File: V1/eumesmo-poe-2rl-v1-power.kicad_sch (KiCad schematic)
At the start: 31 parts, among them U4 TPS2376DDAR-H, U5 TX4138, U6 SY8089A1AAC

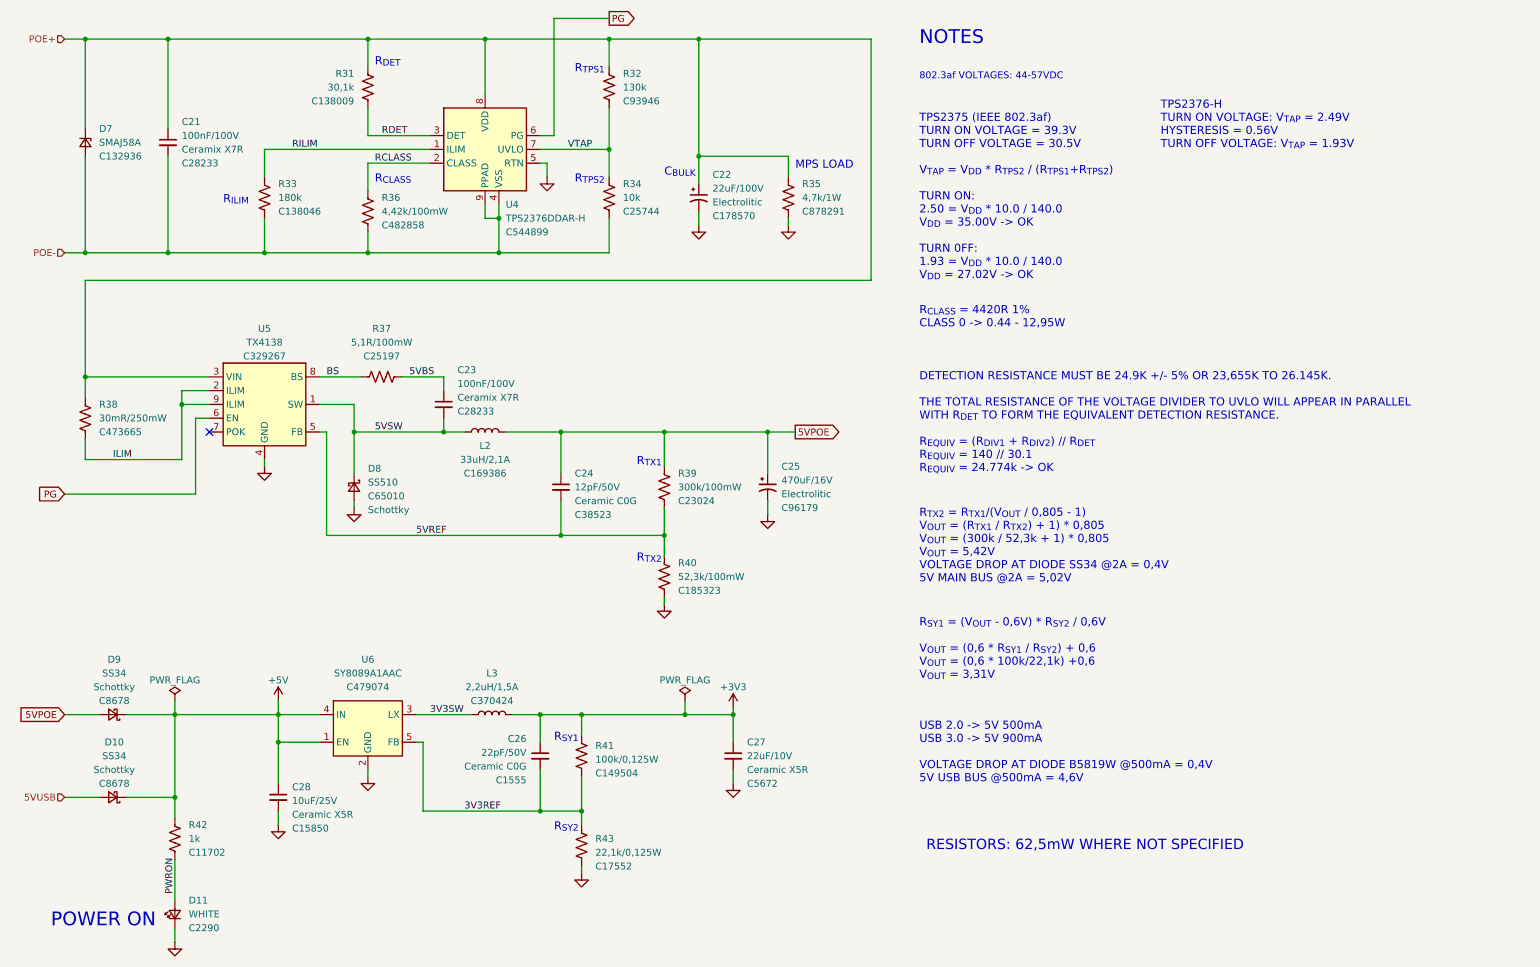
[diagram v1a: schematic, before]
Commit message: Added CPU health LED
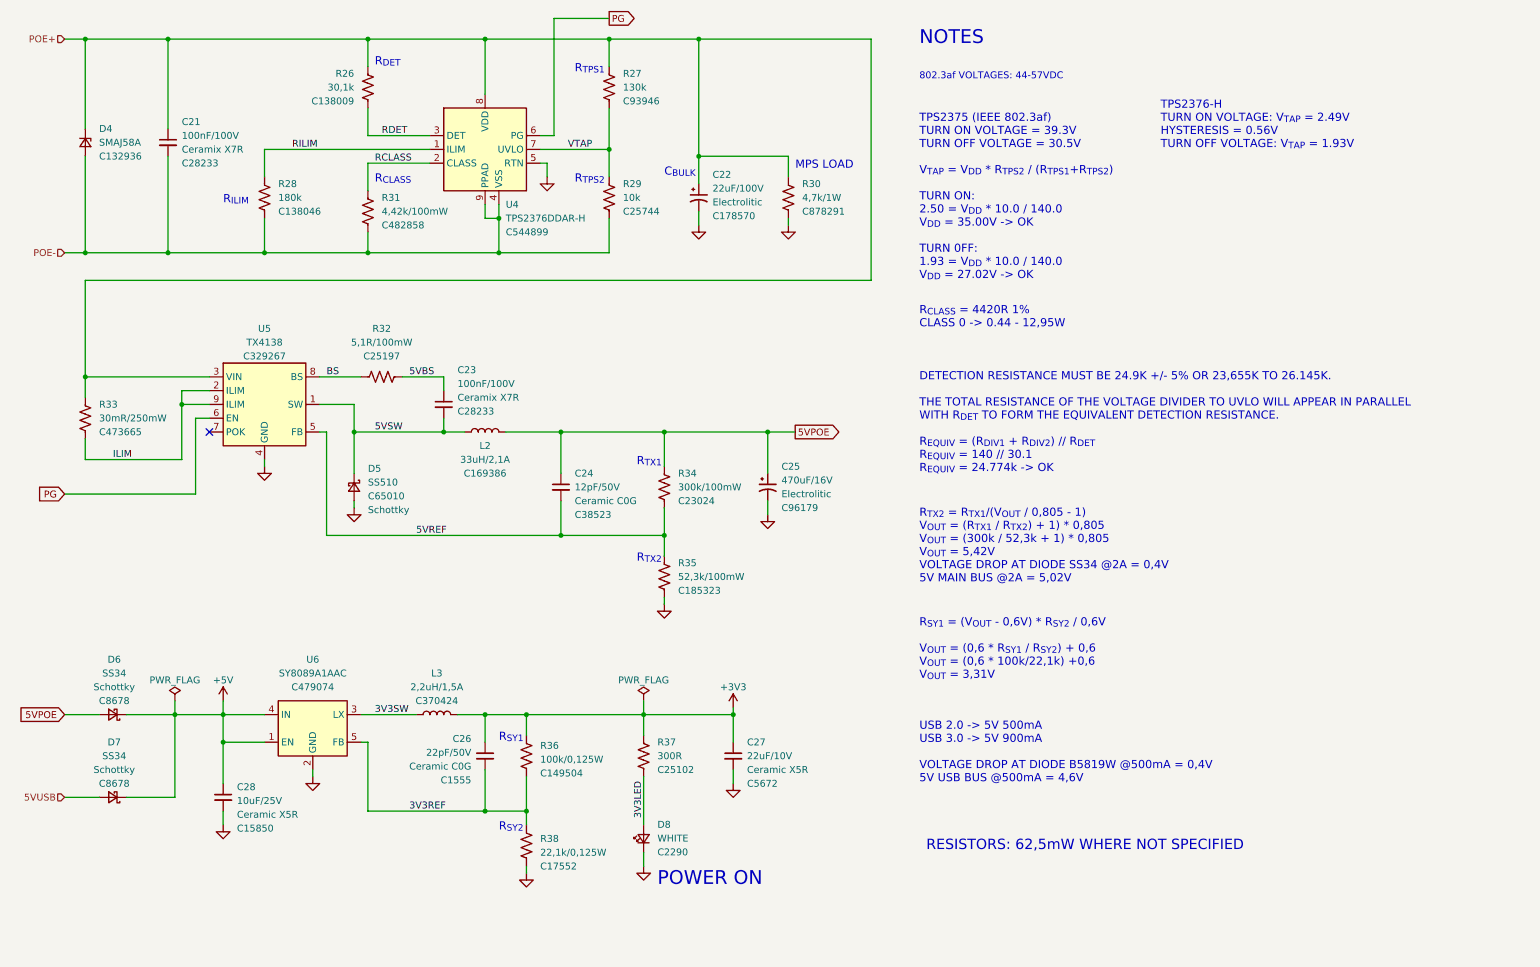
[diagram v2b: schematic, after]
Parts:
- removed D11: WHITE, Tales:LED_0603_1608Metric, symbol Device:LED_Small
- removed R42: 1k, Tales:R_0402_1005Metric, symbol Device:R_US
- added D8: WHITE, Tales:LED_0603_1608Metric, symbol Device:LED_Small
- added R37: 300R, Tales:R_0402_1005Metric, symbol Device:R_US
- renumbered D7 to D4, D8 to D5, D9 to D6, D10 to D7, R31 to R26, R32 to R27, R33 to R28, R34 to R29, R35 to R30, R36 to R31, R37 to R32, R38 to R33, R39 to R34, R40 to R35, R41 to R36, R43 to R38
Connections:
- net +3V3: now also R37.1
- net GND: now also D8.1 (K)
- new net 3V3LED: D8.2 (A), R37.2
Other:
- moved on the sheet: C26, C28, L3, R36, R38, U6
